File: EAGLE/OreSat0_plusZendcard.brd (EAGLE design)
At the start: 99.8 x 94.7 mm, 24 parts, among them J1 Harwin M55-7101242R, J2 Harwin M55-7101242R, J3 Harwin M55-7101242R, J4 Harwin M55-7101242R, J6 J-SAMTEC-TFM-120-X1-XXX-D-RA

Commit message: SHIP IT
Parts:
- added R4: HOT, oresat-rcl:0309/12
- added R5: WARMISH, oresat-rcl:0309/12
- U$4, U$5, U$6, U$7, U$8: value U.FL-PR-SMT -> R107064070_CONTACT; device J-HRS-U.FL-PR-SMT2.5-1(10)-F-RF:U.FL-PR-SMT -> J-Radiall-R107064070-RF:R107064070_CONTACT
- moved U$5 40.5 mm to (73.0, 26.8), turned to 135 degrees
- moved U$6 40.5 mm to (26.8, 26.8), turned to 225 degrees
- moved U$8 40.5 mm to (73.0, 73.0), turned to 45 degrees
- moved U$7 40.5 mm to (26.8, 73.0), turned to 315 degrees
- moved U$4 3.00 mm to (83.9, 80.0), turned to 180 degrees
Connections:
- net GND: now also R4.1, R5.1; no longer U$5.P$2, U$5.P$3, U$6.P$2, U$6.P$3
- net TURNSTILE-DEPLOY: now also R4.2, R5.2
- net UHF_0: now also U$8.P$1; no longer U$5.P$1
- net UHF_180: now also U$6.P$1; no longer U$7.P$1
- net UHF_270: now also U$5.P$1; no longer U$8.P$1
- net UHF_90: now also U$7.P$1; no longer U$6.P$1
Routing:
- net TURNSTILE-DEPLOY: track 1.27 -> 47.4 mm
- net N$12: track 5.92 -> 4.42 mm
- net UHF_90: track 2.96 -> 1.90 mm
- net UHF_180: track 2.96 -> 1.91 mm
- net UHF_0: track 2.96 -> 1.91 mm
- net UHF_270: track 2.96 -> 1.91 mm
- net GND: vias 306 -> 300

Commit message: error correction
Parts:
- R1, R2, R3: value (none) -> 50
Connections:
- net GND: now also U$5.P$2, U$5.P$3, U$6.P$2, U$6.P$3
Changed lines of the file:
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@@
 <attribute name="NAME" x="7.4" y="85.785" locked="yes" size="0.635" layer="25" font="vector" ratio="20" rot="R90"/>
 </element>
-<element name="R1" library="oresat-rcl" package=".0805-B-NOSILK" value="" x="64.1" y="47.15" smashed="yes" rot="MR180">
+<element name="R1" library="oresat-rcl" package=".0805-B-NOSILK" value="50" x="64.1" y="47.15" smashed="yes" rot="MR180">
 <attribute name="NAME" x="62.6" y="46.15" size="0.8" layer="26" font="vector" ratio="15" rot="MR180"/>
 <attribute name="NAME" x="64.1" y="47.15" size="0.4" layer="34" ratio="15" rot="MR180" align="center"/>
 <attribute name="VALUE" x="62.6" y="48.95" size="0.8" layer="28" font="vector" ratio="15" rot="MR180"/>
 </element>
-<element name="R2" library="oresat-rcl" package=".0805-B-NOSILK" value="" x="61.1" y="44.8" smashed="yes" rot="MR0">
+<element name="R2" library="oresat-rcl" package=".0805-B-NOSILK" value="50" x="61.1" y="44.8" smashed="yes" rot="MR0">
 <attribute name="NAME" x="62.6" y="45.8" size="0.8" layer="26" font="vector" ratio="15" rot="MR0"/>
 <attribute name="NAME" x="61.1" y="44.8" size="0.4" layer="34" ratio="15" rot="MR0" align="center"/>
 <attribute name="VALUE" x="62.6" y="43" size="0.8" layer="28" font="vector" ratio="15" rot="MR0"/>
 </element>
-<element name="R3" library="oresat-rcl" package=".0805-B-NOSILK" value="" x="38.2" y="55" smashed="yes" rot="MR180">
+<element name="R3" library="oresat-rcl" package=".0805-B-NOSILK" value="50" x="38.2" y="55" smashed="yes" rot="MR180">
 <attribute name="NAME" x="36.7" y="54" size="0.8" layer="26" font="vector" ratio="15" rot="MR180"/>
 <attribute name="NAME" x="38.2" y="55" size="0.4" layer="34" ratio="15" rot="MR180" align="center"/>
@@
 <via x="80.5" y="76.8" extent="1-16" drill="0.254"/>
 <via x="76.7" y="74.7" extent="1-16" drill="0.254"/>
+<contactref element="U$5" pad="P$2"/>
+<contactref element="U$5" pad="P$3"/>
+<contactref element="U$6" pad="P$2"/>
+<contactref element="U$6" pad="P$3"/>
 </signal>
 <signal name="N$4">

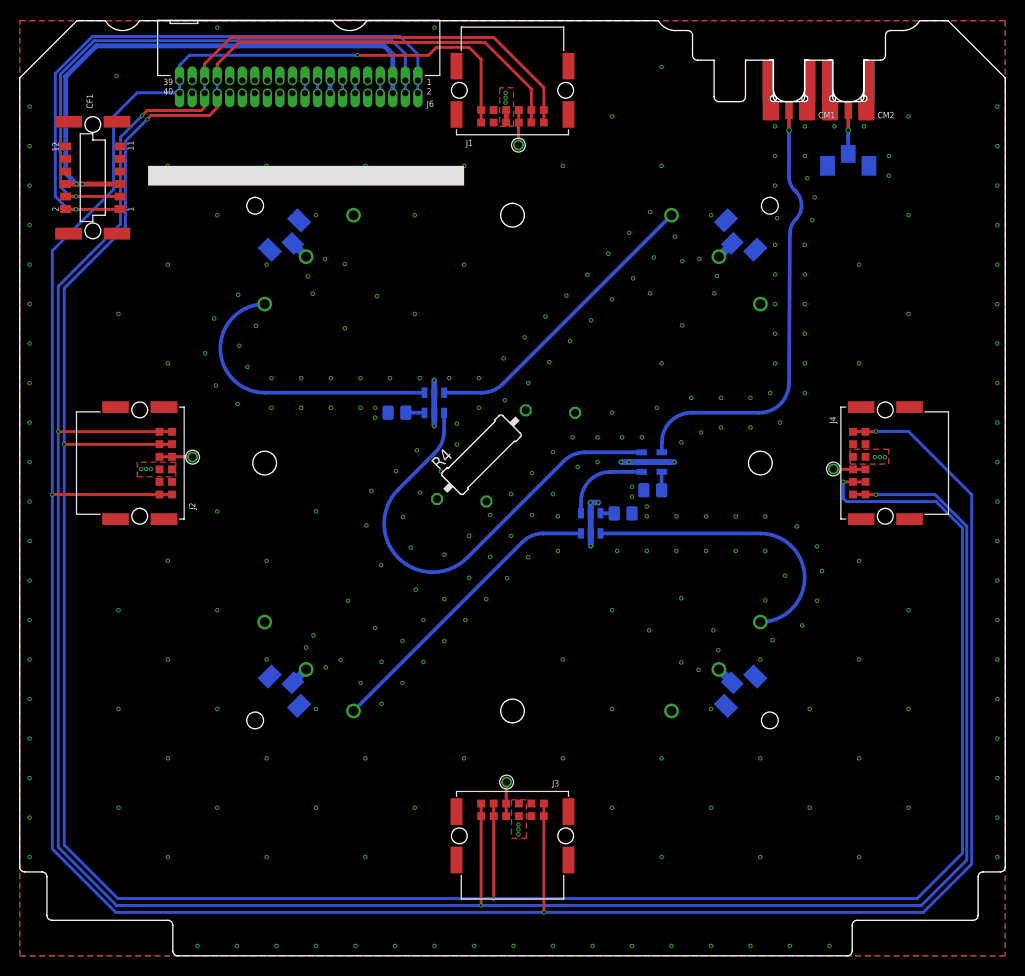
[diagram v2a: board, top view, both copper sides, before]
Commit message: Design review cleanup of Eric's perfectly decent board. Added RF class, moved burnwires for maximum OCD placement, cleaned up schematic a little bit.
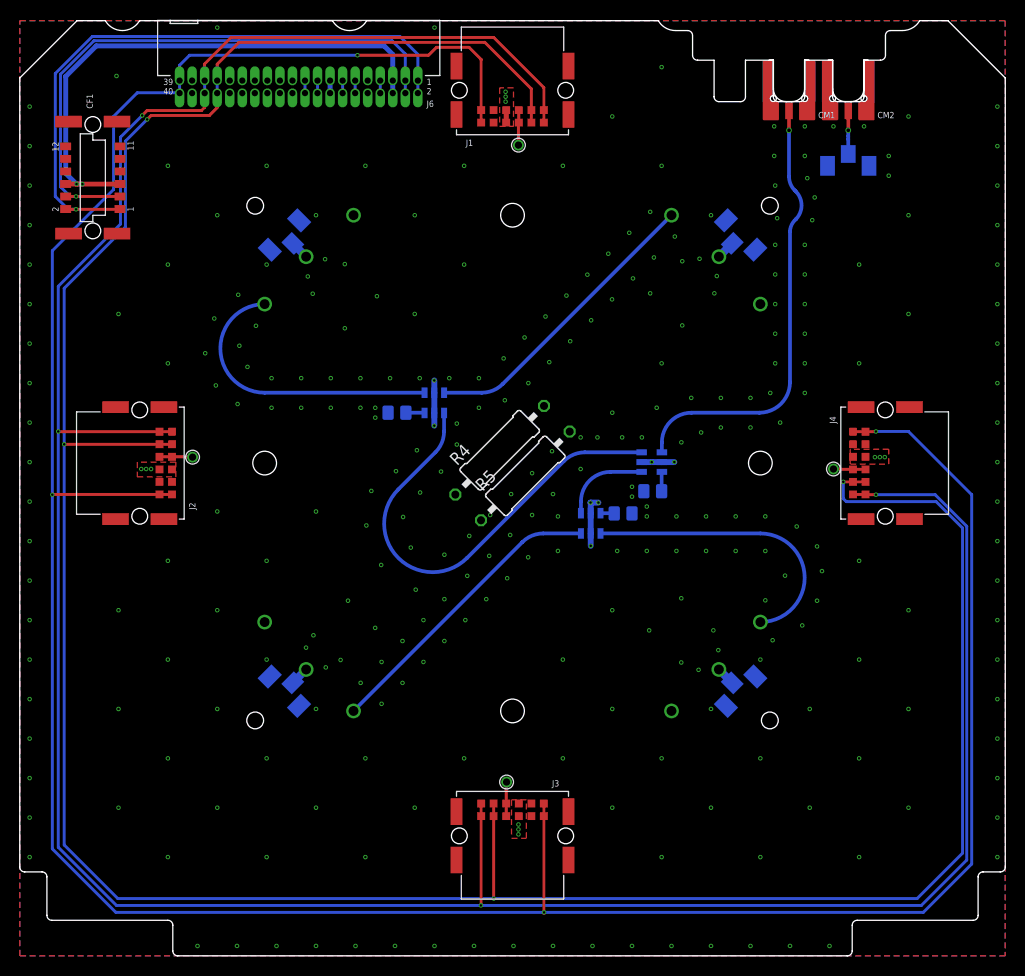
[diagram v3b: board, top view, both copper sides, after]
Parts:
- moved R5 1.98 mm to (51.2, 48.6), flipped to the top, turned to 45 degrees
- moved R4 1.90 mm to (48.6, 51.2)
- moved R1 0.10 mm to (64.1, 47.0)
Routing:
- net TURNSTILE-DEPLOY: track 47.4 -> 0.00 mm
- net GND: track 15.2 -> 13.1 mm, vias 300 -> 298
- added copper zone on layer 2, net TURNSTILE-DEPLOY

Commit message: rerouted mezzanine
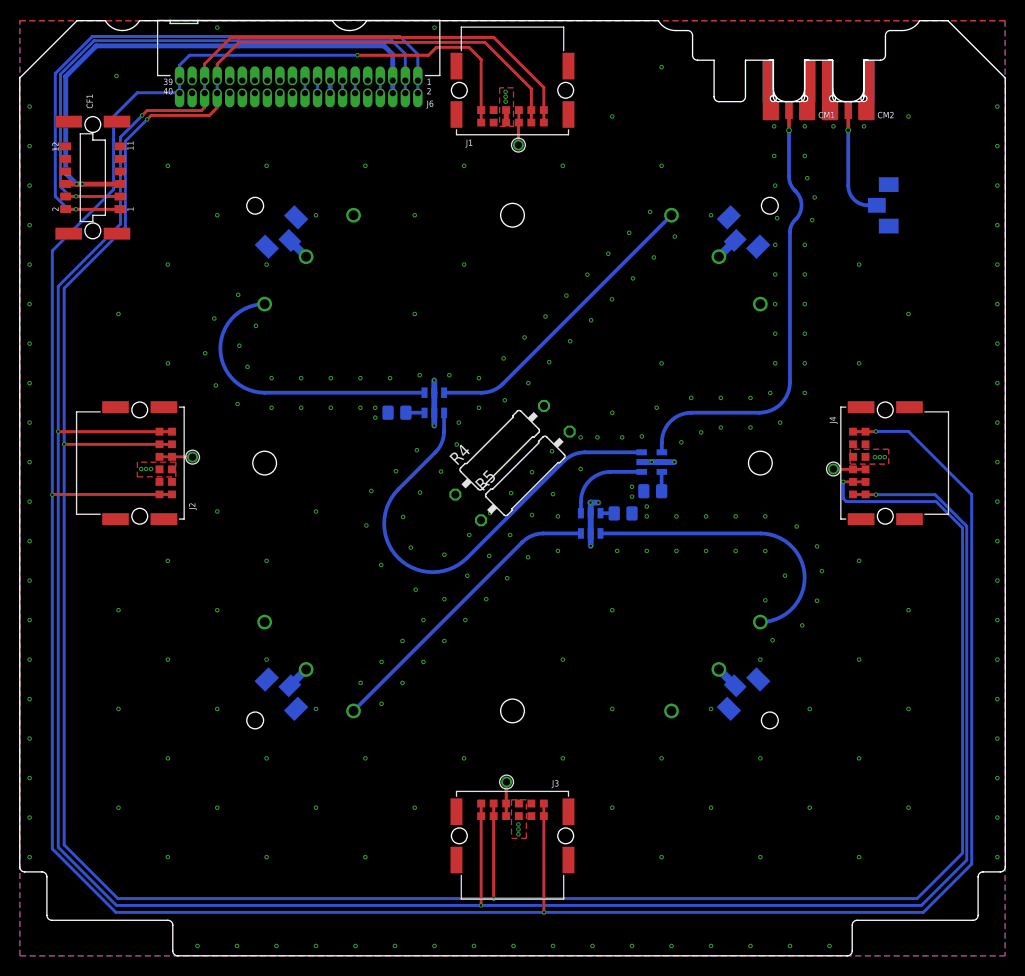
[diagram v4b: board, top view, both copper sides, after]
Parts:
- moved U$4 5.73 mm to (88.0, 76.0), turned to 90 degrees
- moved U$6 0.42 mm to (26.5, 26.5)
- moved U$5 0.42 mm to (73.3, 26.5)
- moved U$7 0.42 mm to (26.5, 73.3)
- moved U$8 0.42 mm to (73.3, 73.3)
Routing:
- net N$12: track 4.42 -> 11.3 mm
- net GND: vias 298 -> 271

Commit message: Minor additions to Eric's lovely boards: Made SD more robust (double vias) with larger isolate, added thicker traces and vias to solar grounds, and chose actual fasteners for the mezzanine board, which includes precision shoulder bolts for the X axis bolts and regularM2 bolts for the Y axis fasteners. Added restricts and STOPs as necessary; note that we kept the top layer under the bolt heads to actually ground them this time - since this is the ground plane of the turnstile, might as well ground all the metal. The fastener stack isn't grounded anywhere else.
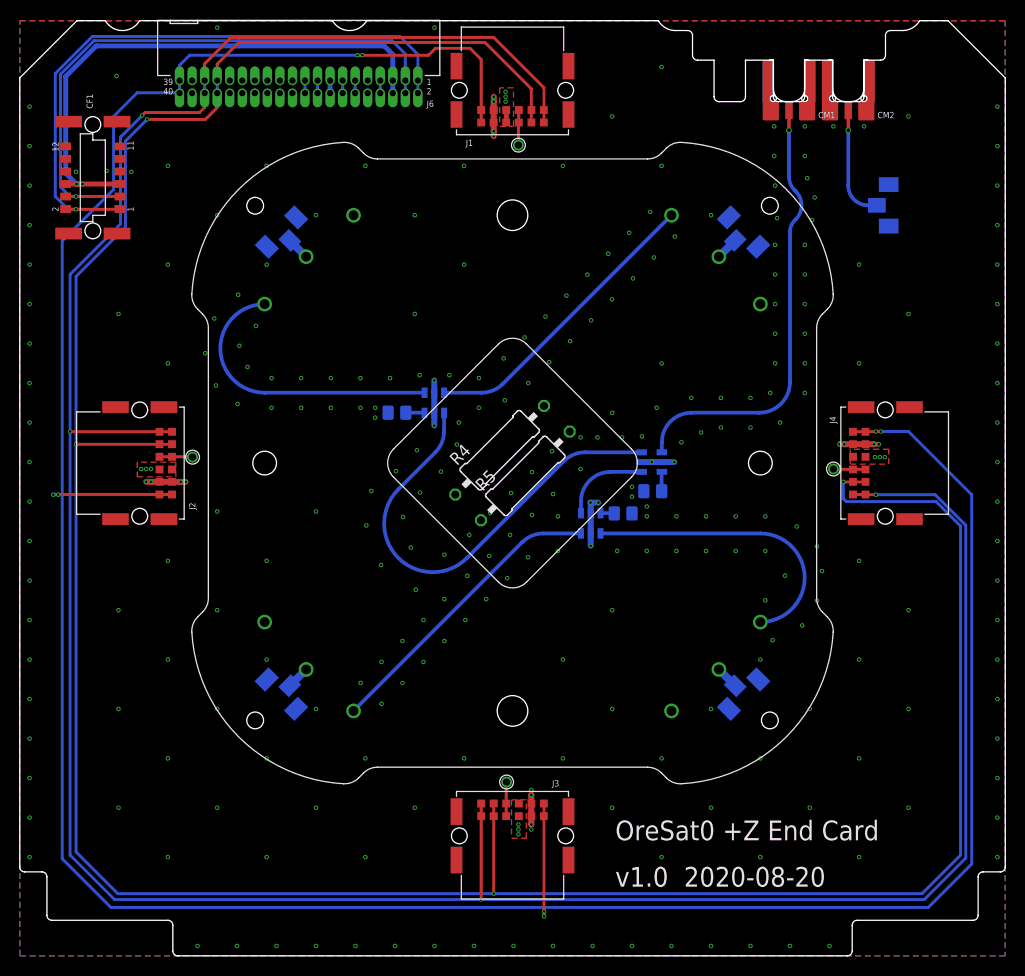
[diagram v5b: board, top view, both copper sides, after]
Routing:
- net GND: track 13.1 -> 27.2 mm, vias 271 -> 290
- net CAN1_L: track 294.7 -> 290.9 mm
- net CAN1_H: track 292.9 -> 289.3 mm
- net !SD: track 298.7 -> 300.3 mm, vias 4 -> 8
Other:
- board text added: "OreSat0 +Z End Card"
- board text added: "v1.0 2020-08-20"

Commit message: Updated some parts to have attributes assigned
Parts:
- removed CM1: J-MOLEX-SMPM-73300-003X_J-MOLEX-SMPM-73300-003X, J-Molex-SMPM-73300-003X:J-MOLEX-SMPM-73300-003X_J-MOLEX-SMPM-073300-003X
- added CM3: J-MOLEX-SMPM-73300-003X, J-Molex-SMPM-73300-003X:J-MOLEX-SMPM-73300-003X
- CM2: value J-MOLEX-SMPM-73300-003X_J-MOLEX-SMPM-73300-003X -> J-MOLEX-SMPM-73300-003X; device J-Molex-SMPM-73300-003X:J-MOLEX-SMPM-73300-003X_J-MOLEX-SMPM-073300-003X -> J-Molex-SMPM-73300-003X:J-MOLEX-SMPM-73300-003X
- moved CM2 6.00 mm to (77.9, 90.7)
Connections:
- net GND: now also CM3.P$1, CM3.P$2, CM3.P$3, CM3.P$4; no longer CM1.P$1, CM1.P$2, CM1.P$3, CM1.P$4
- net N$1: now also CM2.RF; no longer CM1.RF
- net N$12: now also CM3.RF; no longer CM2.RF

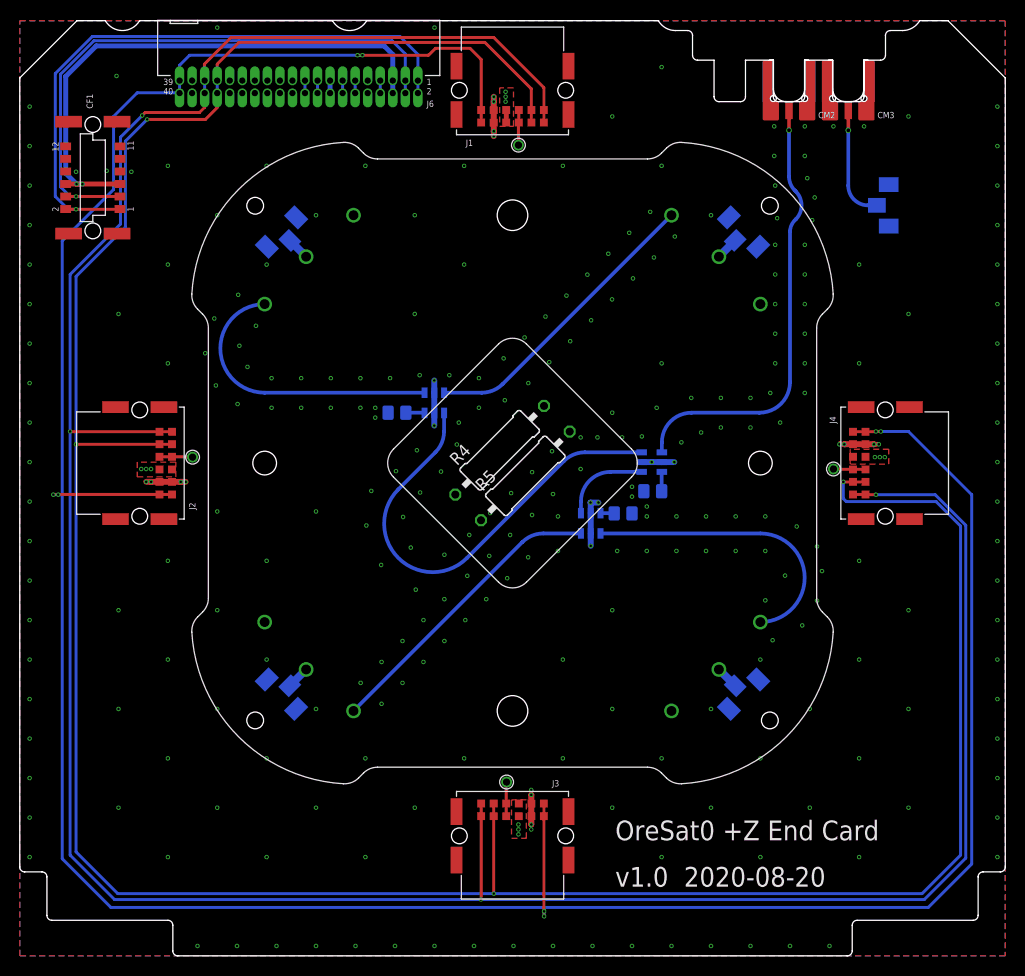
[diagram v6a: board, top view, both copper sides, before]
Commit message: +Z end card new outline and fasteners
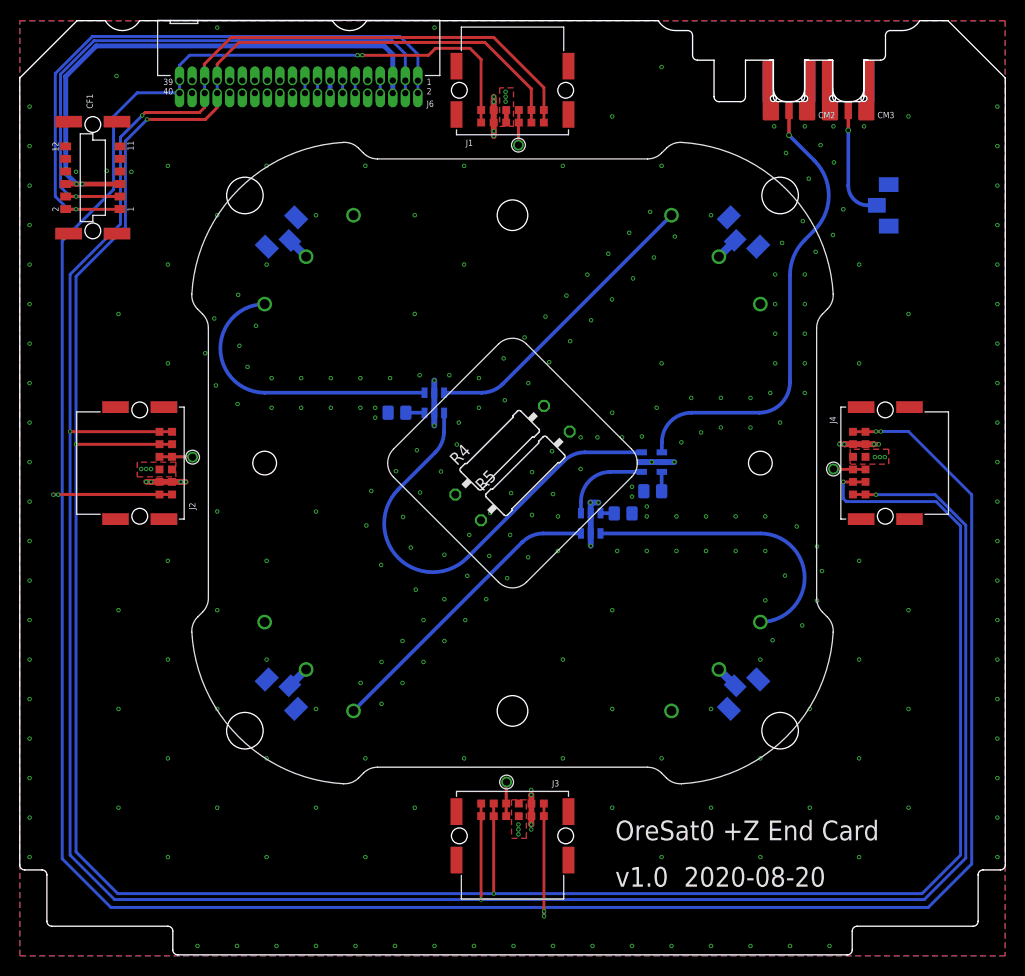
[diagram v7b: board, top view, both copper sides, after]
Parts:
- added U$10, U$11, U$12, U$9: MCMASTER-94100A150, HW-mcmaster-94100A150-M2-threaded-insert:MCMASTER-94100A150
- PCB1: value ORESAT-CARD-V1.1-END-CARD-3RF-V1.0 -> ORESAT-CARD-V1.3-END-CARD-3RF-V1.0; device oresat-cards:ORESAT-CARDV1.1-END-CARD-3RF-V1.0 -> oresat-cards:ORESAT-CARD-V1.3-END-CARD-3RF-V1.0
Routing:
- net N$1: track 44.3 -> 45.8 mm
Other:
- board size 99.8 x 94.7 mm -> 99.8 x 94.6 mm
